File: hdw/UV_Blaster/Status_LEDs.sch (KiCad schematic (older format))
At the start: 10 parts

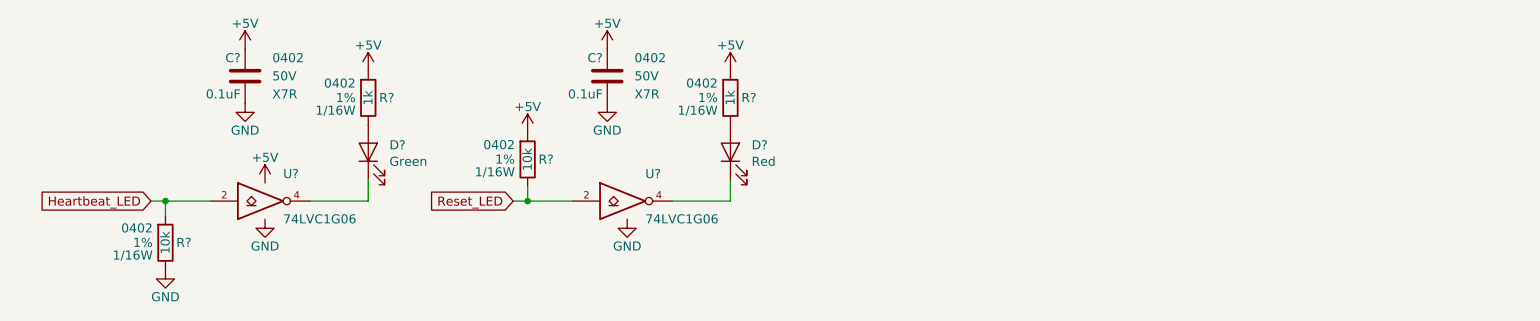
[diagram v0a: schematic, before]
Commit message: More sch work, netlist, part numbers, footprints
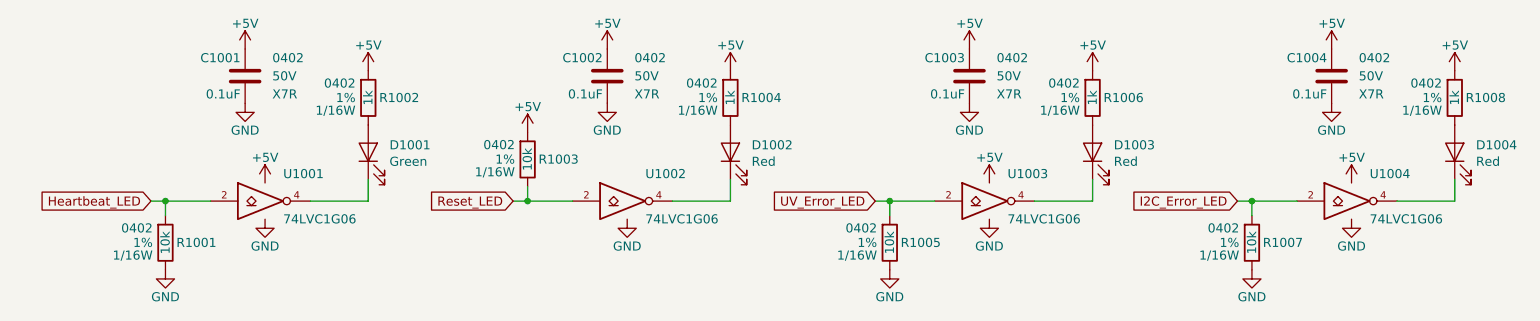
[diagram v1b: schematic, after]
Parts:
- added C1003, C1004: 0.1uF, Capacitors_SMD:C_0402, symbol Custom_Library:C_Custom
- added D1003, D1004: Red, LEDs:LED_0402, symbol Device:LED
- added R1005, R1007: 10k, Resistors_SMD:R_0402, symbol Custom_Library:R_Custom
- added R1006, R1008: 1k, Resistors_SMD:R_0402, symbol Custom_Library:R_Custom
- added U1003, U1004: 74LVC1G06, TO_SOT_Packages_SMD:SOT-353_SC-70-5, symbol Custom_Library:74LVC1G06_Power
- D1001: renamed from D?; footprint (none) -> LEDs:LED_0402; Digi-Key PN (none) -> 754-1815-1-ND
- D1002: renamed from D?; footprint (none) -> LEDs:LED_0402; Digi-Key PN (none) -> 754-1812-1-ND
- R1001, R1003: renamed from R?; Digi-Key PN RMCF0402FT10K0CT-ND -> 541-3959-1-ND
- R1002, R1004: renamed from R?; Digi-Key PN 541-1.00KLCT-ND -> P1.00KLCT-ND
- gave numbers to parts that had none: 4
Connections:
- net +5V: now also C1003.1, C1004.1, R1006.1, R1008.1, U1003.5 (VCC), U1004.5 (VCC)
- net GND: now also C1003.2, C1004.2, R1005.2, R1007.2, U1003.3 (GND), U1004.3 (GND)
- new net: D1003.2 (A), R1006.2
- new net: D1003.1 (K), U1003.4
- new net: D1004.2 (A), R1008.2
- new net: D1004.1 (K), U1004.4
- new net I2C_Error_LED: R1007.1, U1004.2
- new net UV_Error_LED: R1005.1, U1003.2
